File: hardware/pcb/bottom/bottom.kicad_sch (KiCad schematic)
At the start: 47 parts, among them J1 Conn_01x15_Socket

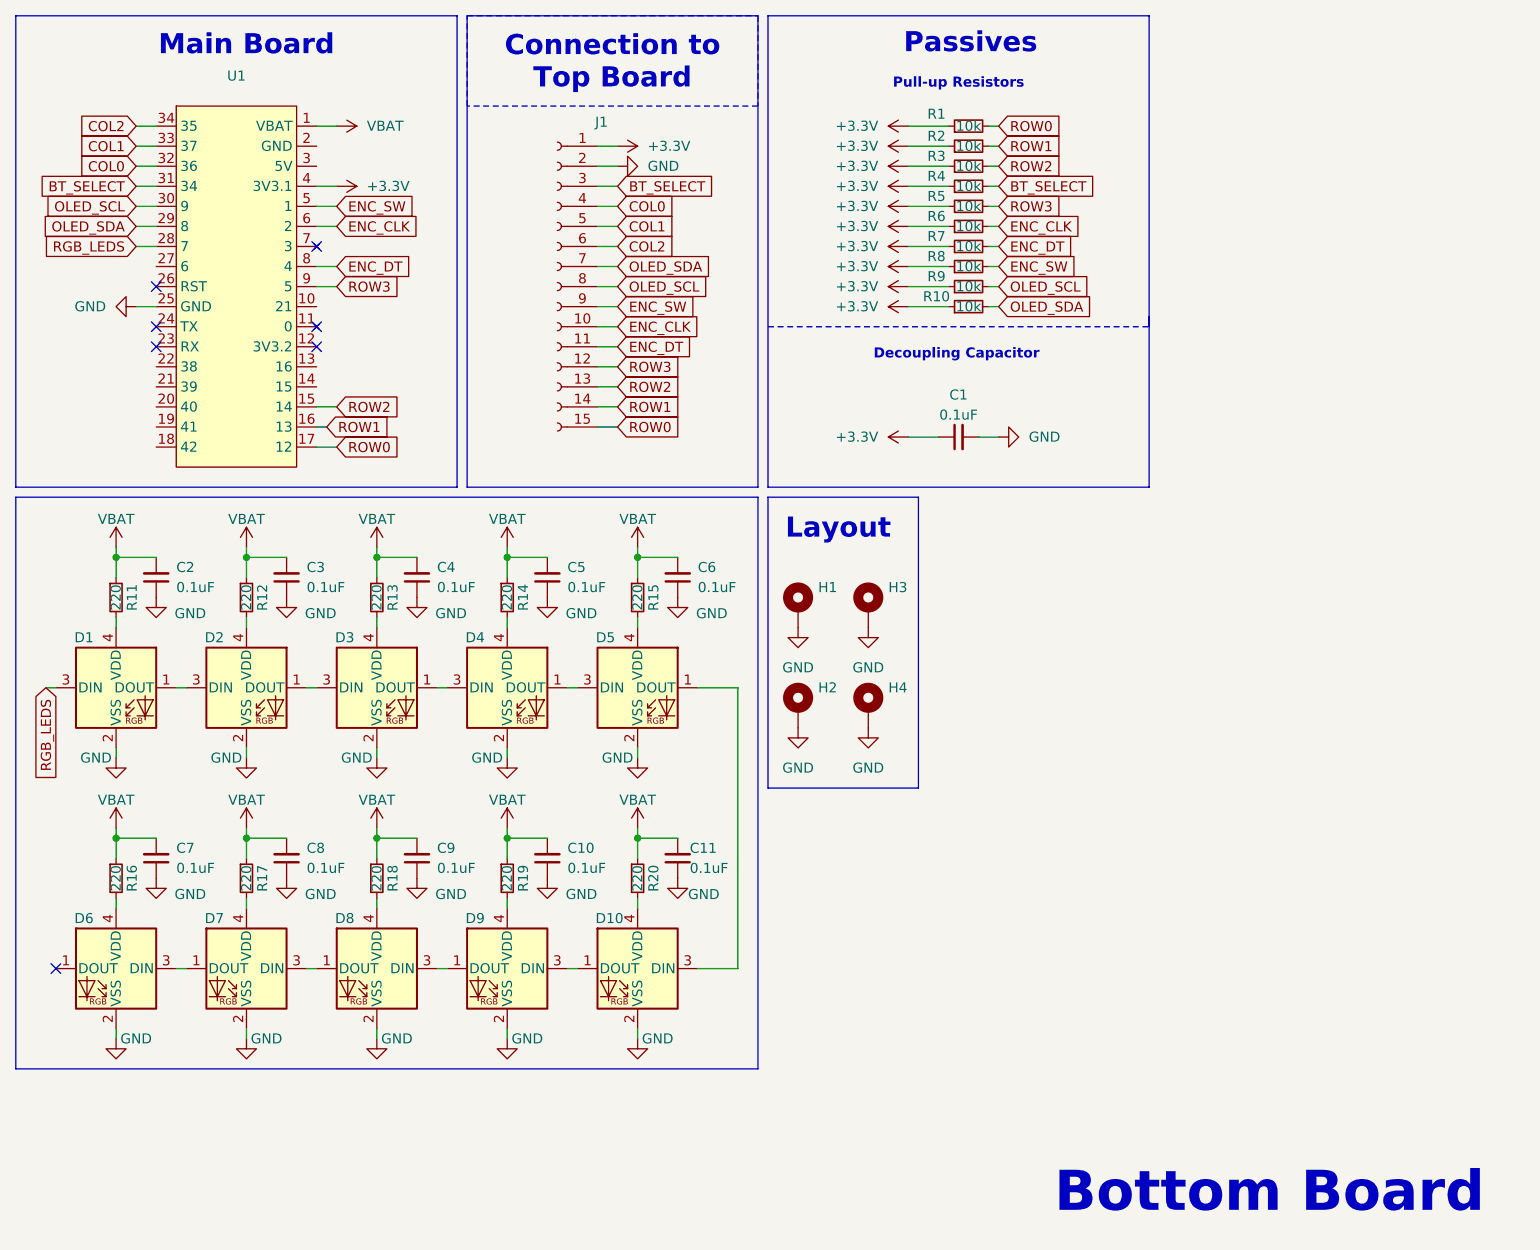
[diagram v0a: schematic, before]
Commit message: Add SOT95P280X145-6N footprint to Bottom-Footprints library
- Created a new footprint for the SOT95P280X145-6N component.
- Included necessary pads, silkscreen, and fabrication lines.
- Added 3D model reference for TPS22918DBVR.
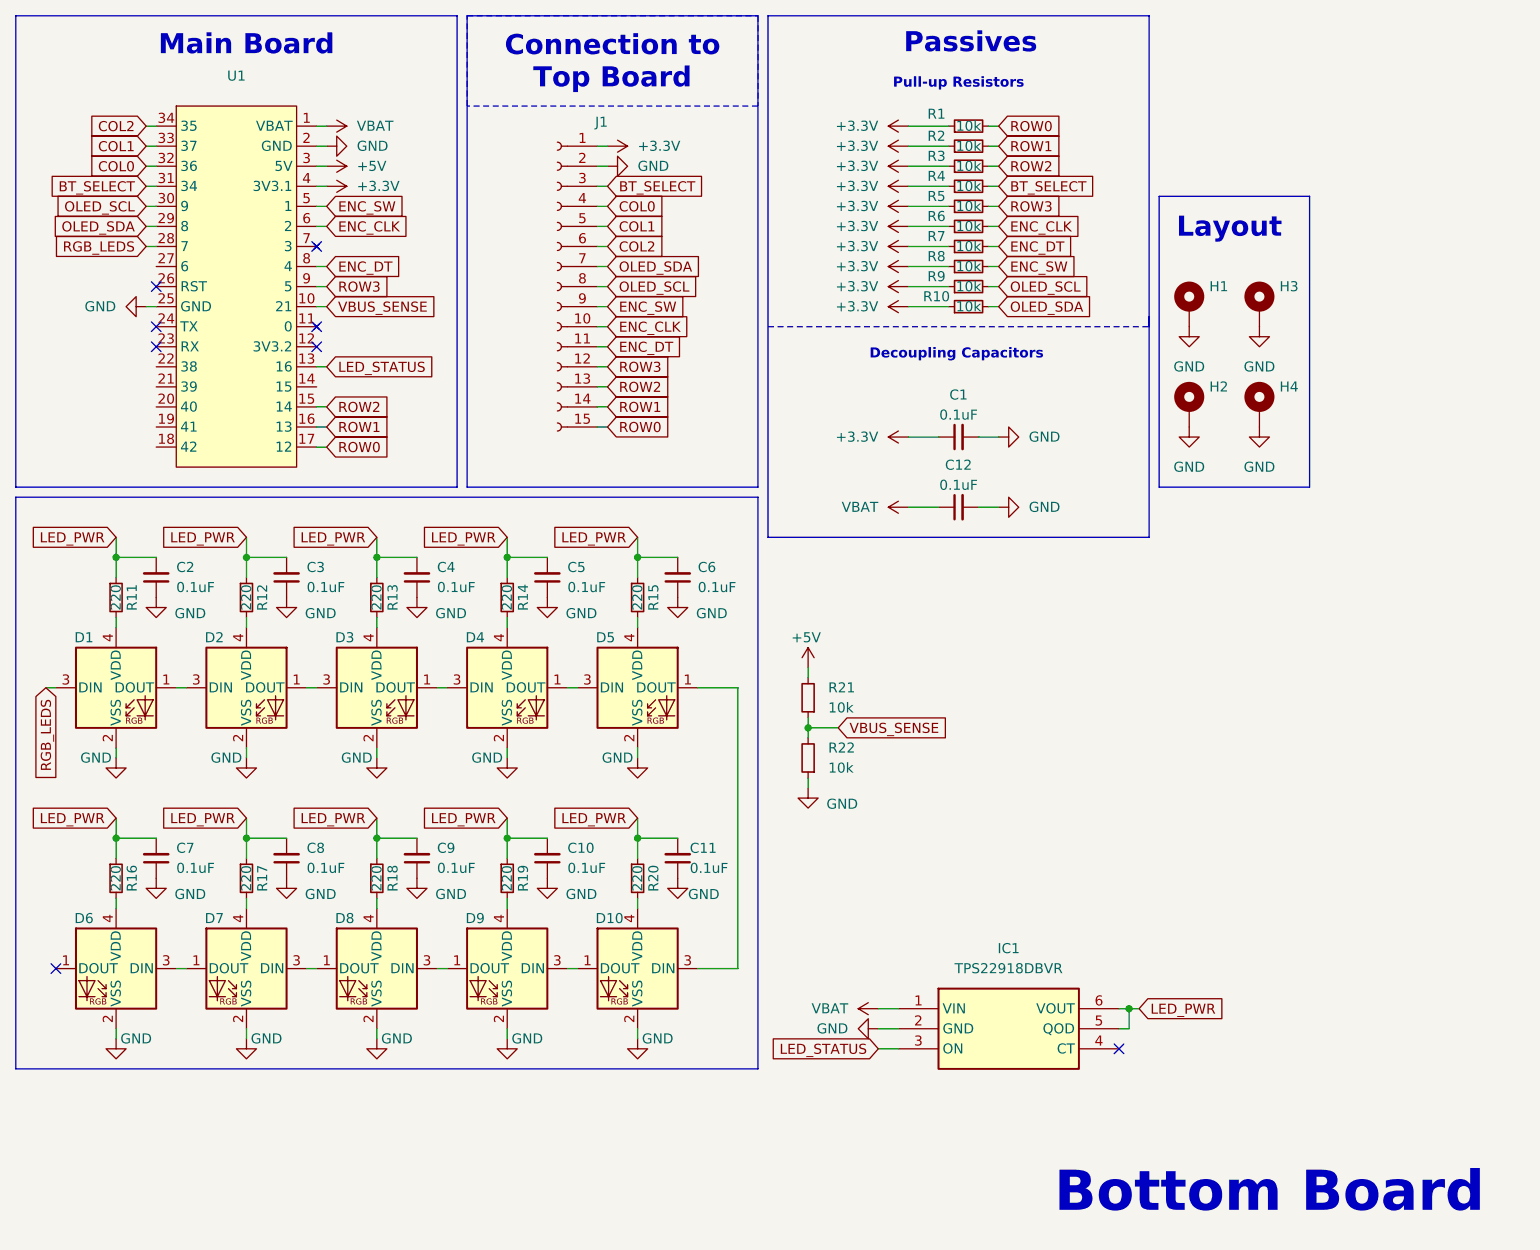
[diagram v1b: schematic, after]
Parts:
- added C12: 0.1uF, Bottom-Footprints:C_0805_2012Metric_Pad1.18x1.45mm_HandSolder, symbol Bottom-Symbols:C_Small
- added IC1: TPS22918DBVR, Bottom-Footprints:SOT95P280X145-6N, symbol Bottom-Symbols:TPS22918DBVR
- added R21, R22: 10k, Bottom-Footprints:R_0805_2012Metric_Pad1.20x1.40mm_HandSolder, symbol Bottom-Symbols:R_Small
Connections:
- net GND: now also U1.2 (GND), C12.2, IC1.2 (GND), R22.1
- net VBAT: now also C12.1, IC1.1 (VIN); no longer C10.2, C11.2, C2.2, C3.2, C4.2, C5.2, C6.2, C7.2, C8.2, C9.2, R11.1, R12.1, R13.1, R14.1, R15.1, R16.1, R17.1, R18.1, R19.1, R20.1
- net VBUS_SENSE: now reaches U1.10 (21)
- net VBUS_SENSE: now also R21.1, R22.2
- net LED_STATUS: now reaches U1.13 (16)
- net LED_STATUS: now also IC1.3 (ON)
- net +5V: now reaches U1.3 (5V)
- net +5V: now also R21.2
- new net LED_PWR: C10.2, C11.2, C2.2, C3.2, C4.2, C5.2, C6.2, C7.2, C8.2, C9.2, IC1.5 (QOD), IC1.6 (VOUT), R11.1, R12.1, R13.1, R14.1, R15.1, R16.1, R17.1, R18.1, R19.1, R20.1
- no-connect marks 7 -> 8
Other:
- note added: "Decoupling Capacitors"
- note removed: "Decoupling Capacitor"
- moved on the sheet: H1, H2, H3, H4

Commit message: update documentation images, remove copper pours and vias from top plate, minor fixes
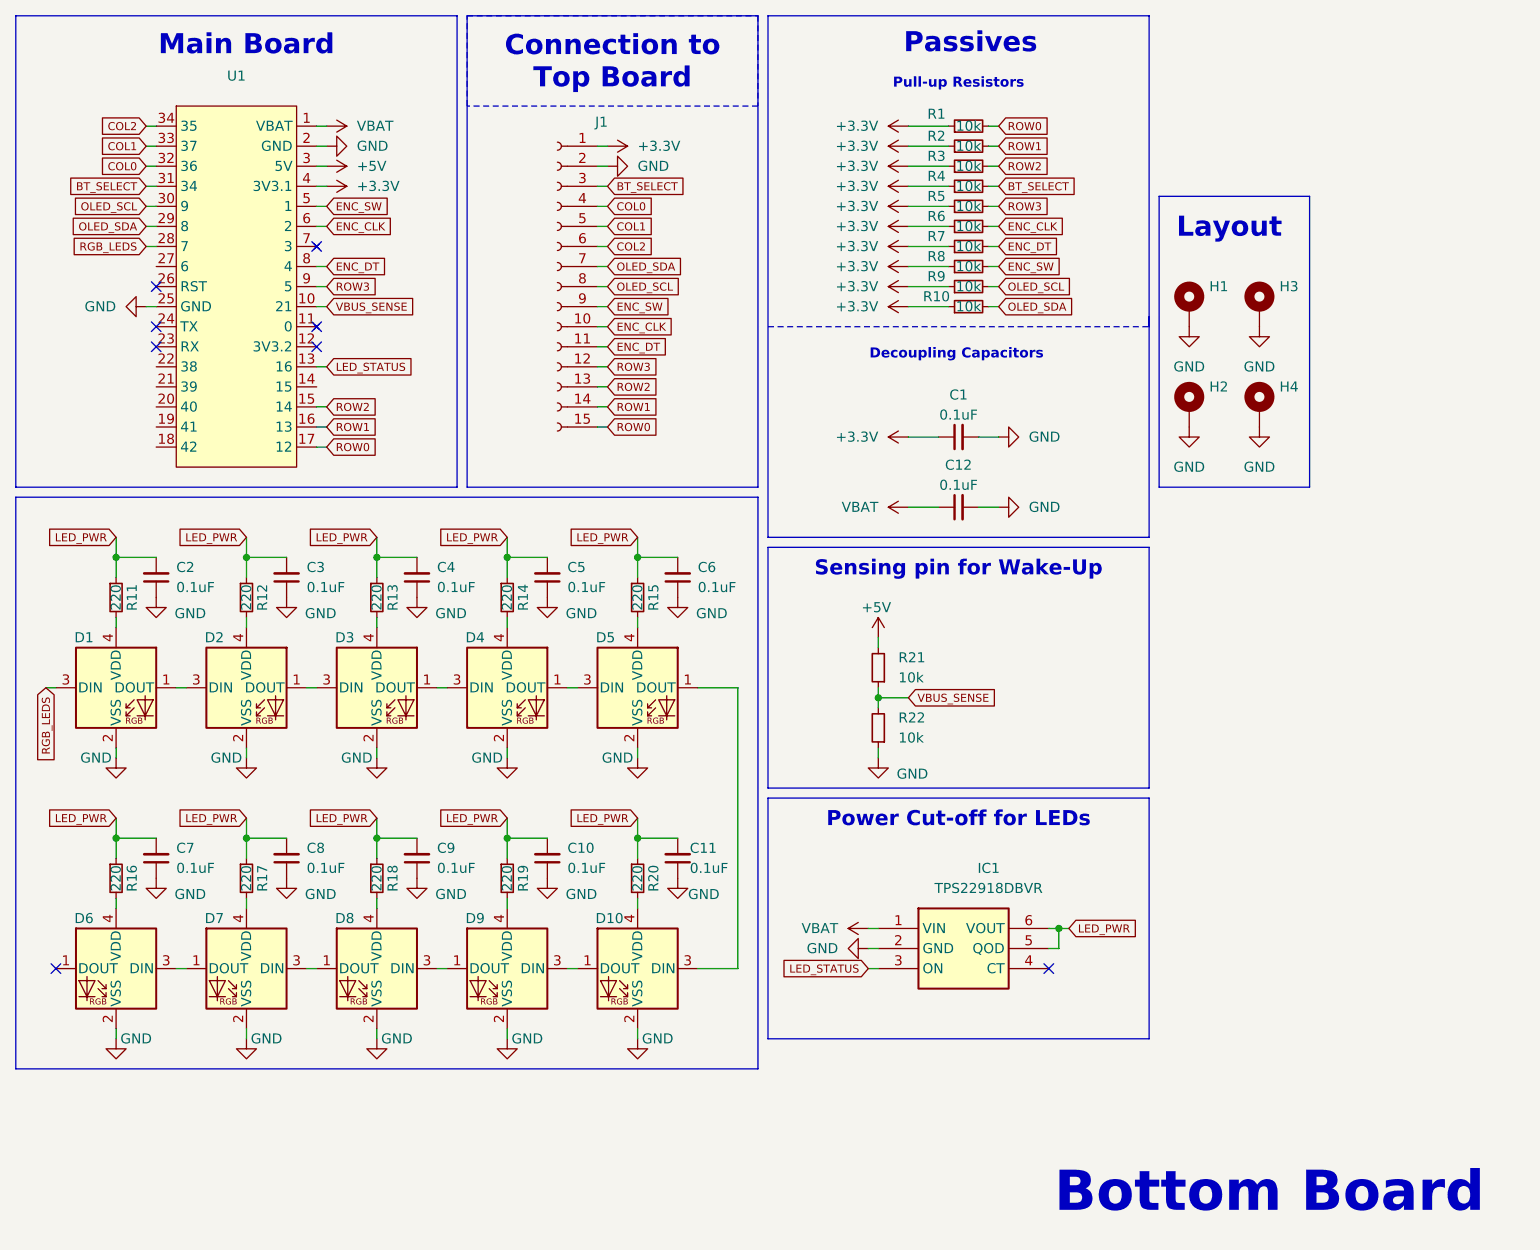
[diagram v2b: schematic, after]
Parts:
- IC1: footprint Bottom-Footprints:SOT95P280X145-6N -> SOT95P280X145-6N
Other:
- moved on the sheet: IC1, R21, R22

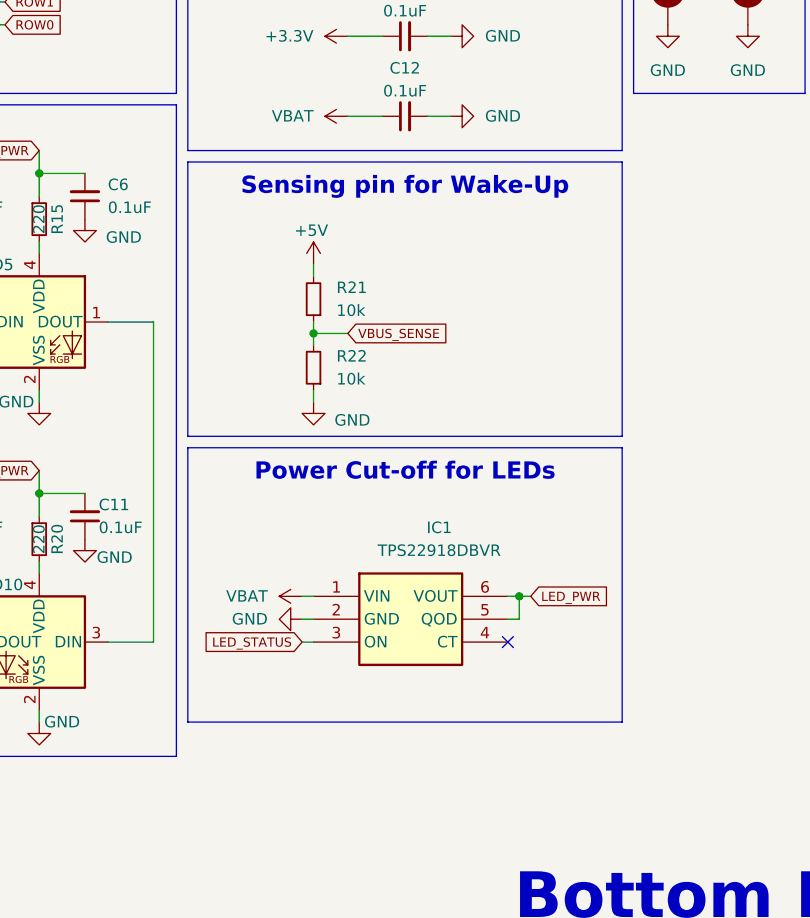
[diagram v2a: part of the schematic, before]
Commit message: changed m2.5 mh to m2, added screws and nuts to enclosure.FCStd
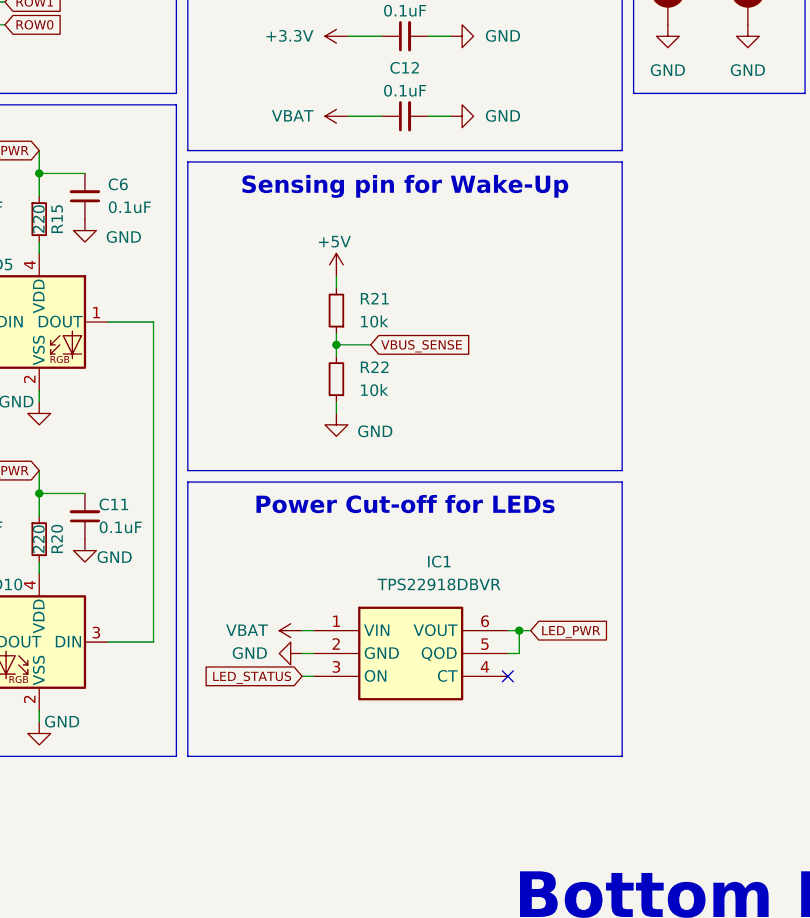
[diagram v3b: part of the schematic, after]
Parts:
- H1, H2, H3, H4: footprint Bottom-Footprints:MountingHole_2.5mm_Pad -> MountingHole:MountingHole_2.2mm_M2_DIN965_Pad
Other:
- moved on the sheet: IC1, R21, R22
